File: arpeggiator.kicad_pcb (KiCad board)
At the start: 2 copper layers, 220 x 170 mm, 360 parts, among them J202 logic test header, J601 3.5mm mono line out, J701 PJ-102AH / 12V DC centre +, Q601 2N7002, Q602 MMBT3904, Q603 BSS84, Q604 MMBT3904, Q605 2N7002, Q606 MMBT3906, Q701 AO3401A, Q702 MMBT3906, Q703 MMBT3906, SW101 C, SW102 C sharp, SW103 D, SW104 D sharp, SW105 E, SW106 F, SW107 F sharp, SW108 G, SW109 G sharp, SW110 A, SW111 A sharp, SW112 B, SW113 start / stop, SW114 1 / 2 / 3 octaves, SW601 saw / pulse, U101 TLC555IDR, U102 TLC555IDR, U103 MCP100T-450I/TT, U201 74HC574, U202 74HC574, U203 74HC574, U204 74HC574, U205 74HC377, U206 74HC377, U211 74HC163, U212 74HC138, U213 74HC163, U214 74HC163, U215 74HC163, U216 CD74HC4067M, U221 74HC377, U222 74HC154, U301 74HC74, U302 74HC74, U303 74HC74, U401 74HC14, U402 74HC14, U403 74HC14, U404 74HC04, U405 74HC04, U406 74HC08, U407 74HC86, U408 74HC04, U409 74HC32, U410 74HC32, U411 74HC32, U412 74HC32, U413 74HC08, U414 74HC08, U415 74HC86, U416 74HC04, U417 74HC08, U418 74HC08, U419 74HC32, U420 74HC14, U421 74HC08, U422 74HC32, U423 74HC08, U424 74HC32, U425 74HC08, U501 OPA4192IDR, U502 ADG706BRUZ, U503 74HC4051D, U504 AS3340A, U601 TLC555IDR, U602 OPA4192IDR, U603 TL074HIDR, U604 LM13700M/NOPB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

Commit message: finish signal routing and clean up the traces
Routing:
- net PITCH0: track 0.00 -> 248.3 mm, vias 0 -> 7
- net PITCH1: track 0.00 -> 228.5 mm, vias 0 -> 9
- net PITCH3: track 0.00 -> 222.4 mm, vias 0 -> 10
- net PITCH2: track 0.00 -> 220.6 mm, vias 0 -> 2
- net OCTAVE0: track 0.00 -> 168.9 mm, vias 0 -> 4
- net TRIGGER: track 0.00 -> 167.5 mm, vias 0 -> 5
- net OCTAVE1: track 0.00 -> 155.2 mm, vias 0 -> 6
- net VALID: track 56.6 -> 195.7 mm, vias 4 -> 5
- net G060: track 0.00 -> 139.0 mm, vias 0 -> 8
- net +5V: track 1531.4 -> 1668.6 mm, vias 26 -> 57
- net N1: track 18.2 -> 151.6 mm, vias 2 -> 5
- net NEG_BAD: track 0.00 -> 118.5 mm, vias 0 -> 4
- net RESET5_N: track 0.00 -> 108.3 mm, vias 0 -> 6
- net G081: track 0.00 -> 99.4 mm, vias 0 -> 8
- net BUTTON_RC: track 27.6 -> 124.2 mm, vias 2 -> 5
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
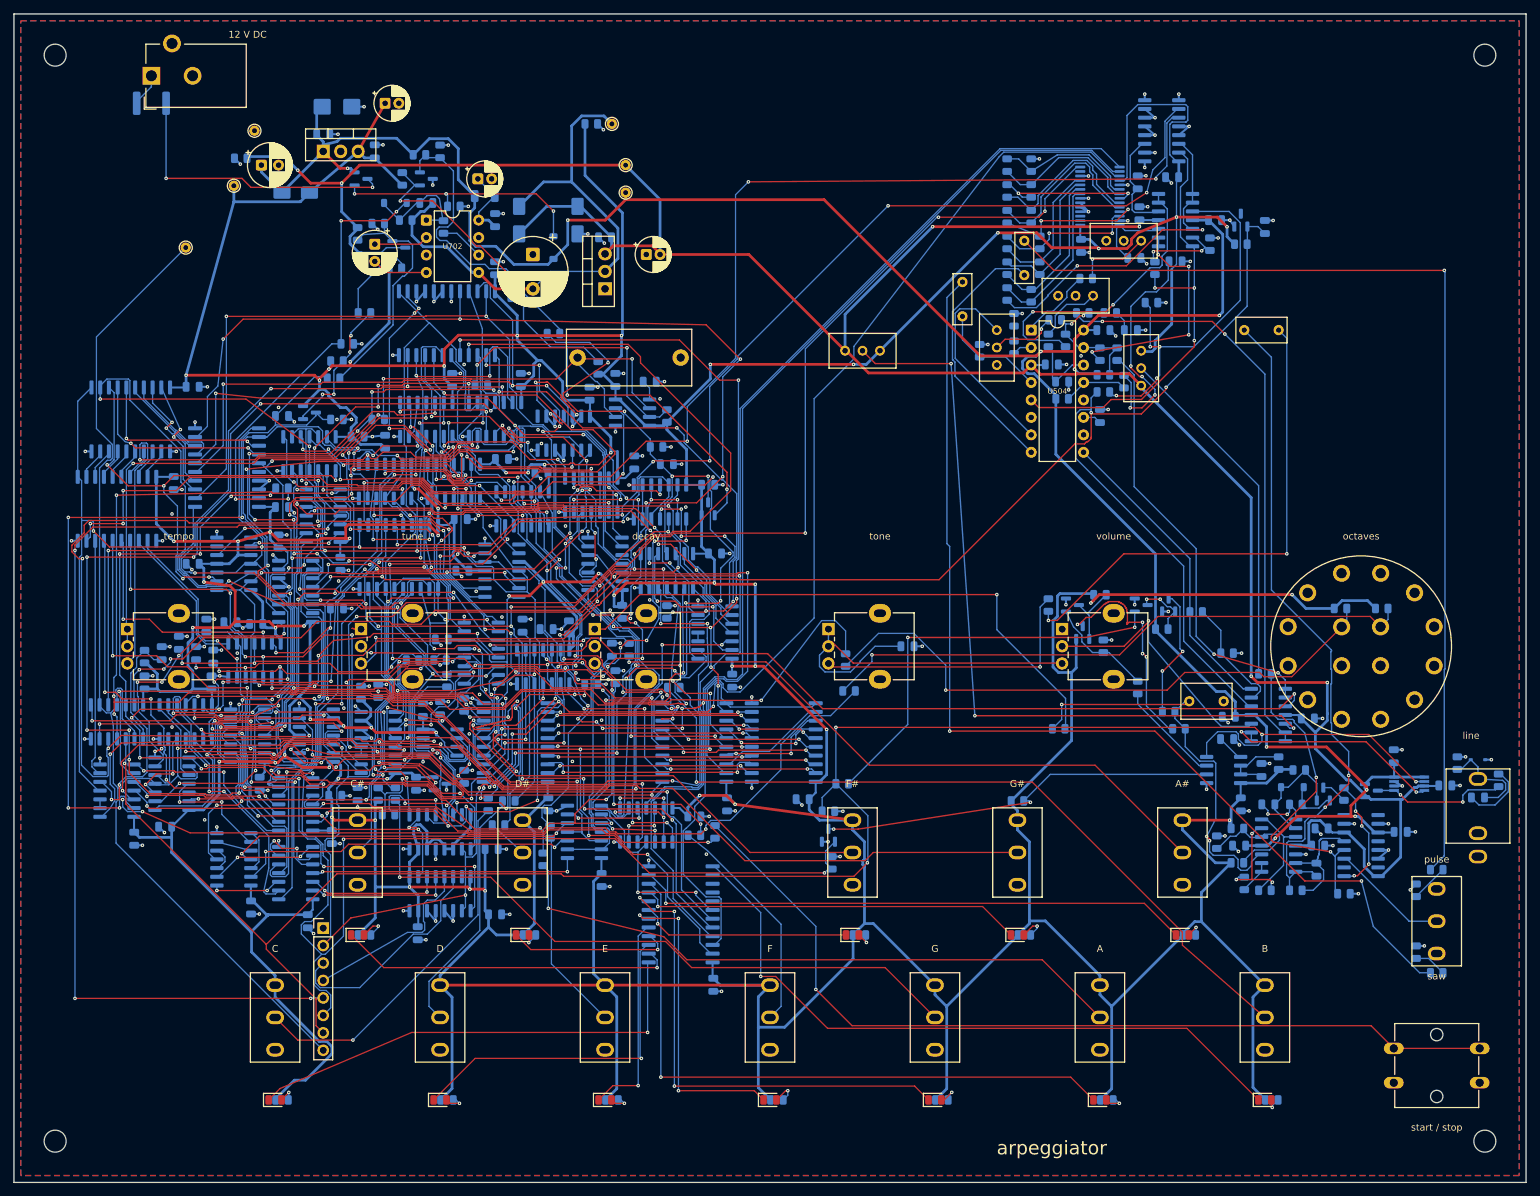
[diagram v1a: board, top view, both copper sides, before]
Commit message: connect ground pours and remove redundant routing
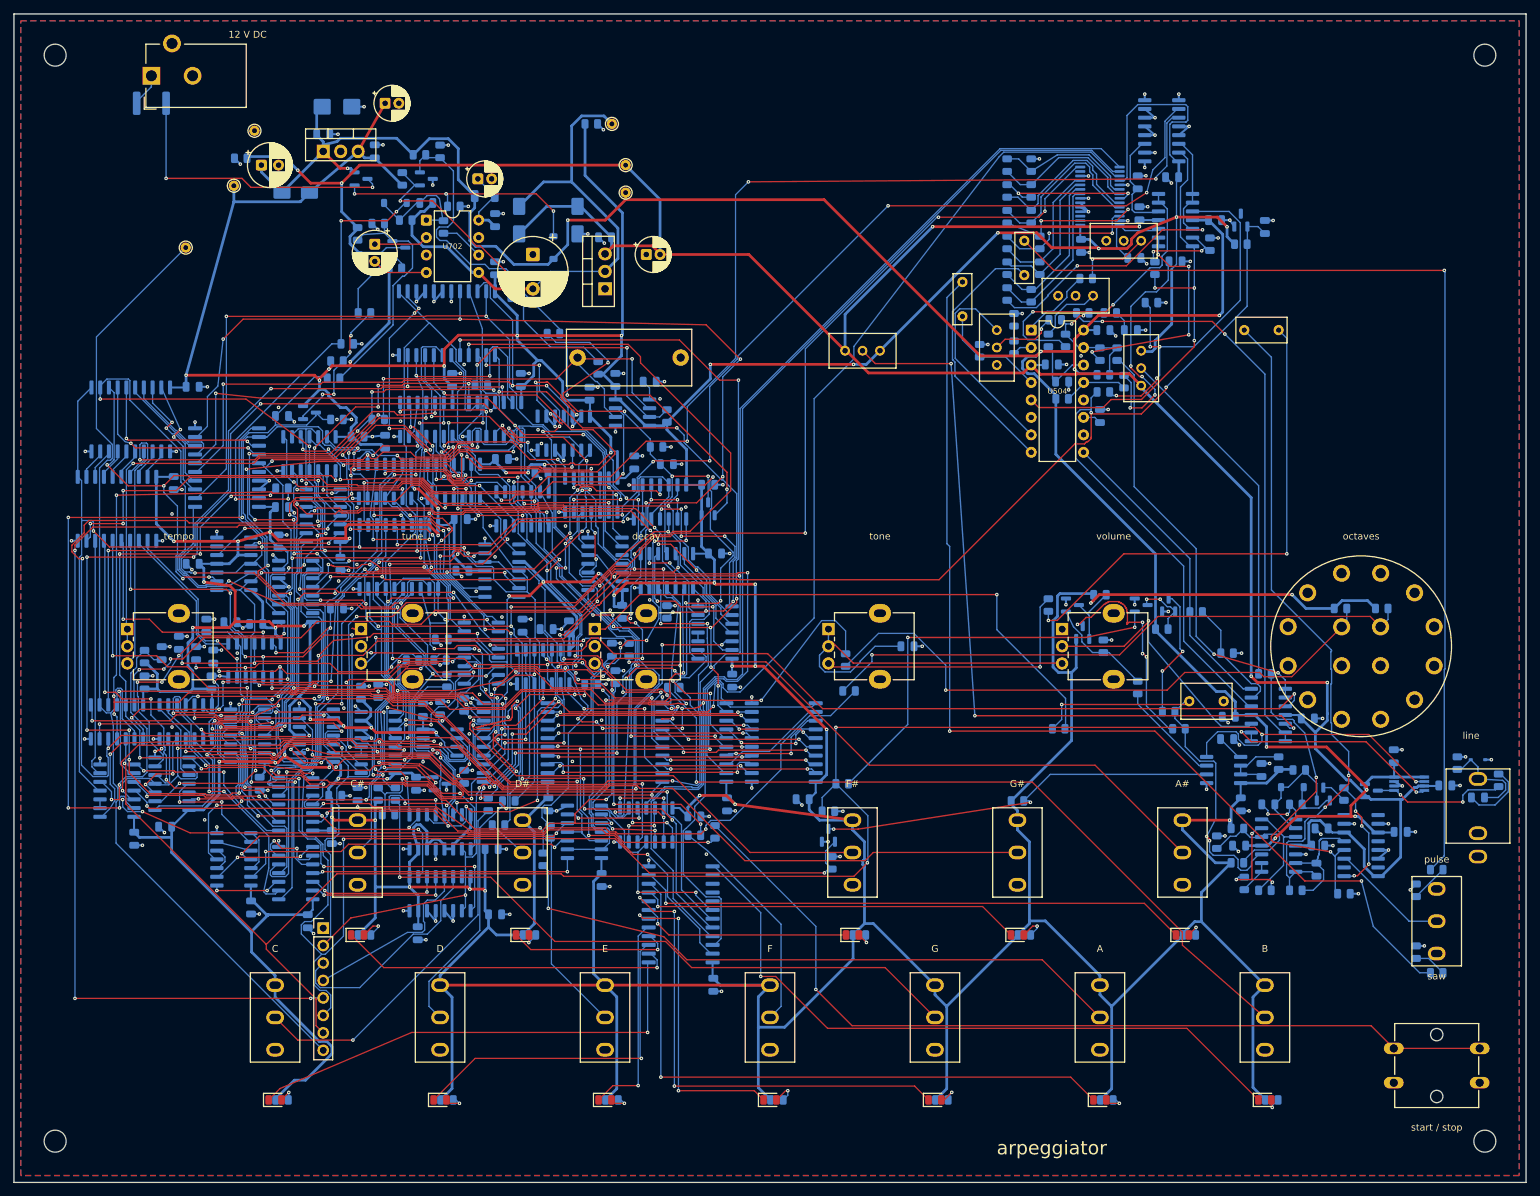
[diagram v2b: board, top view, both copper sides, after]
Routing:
- net FAST_CLK: track 358.8 -> 353.6 mm
- net ADVANCE: track 50.4 -> 47.2 mm
- net RANGE0: track 116.0 -> 113.0 mm
- net N3: track 152.4 -> 149.6 mm
- net RESET_N: track 295.1 -> 292.3 mm
- net RANGE1: track 134.0 -> 131.5 mm
- net N2: track 143.9 -> 141.4 mm
- net TIM161: track 130.0 -> 127.6 mm
- net PITCH1: track 228.5 -> 226.2 mm, vias 9 -> 8
- net RUN: track 158.8 -> 156.6 mm
- net NOTE_SNAP3: track 88.7 -> 86.7 mm
- net OCT_EN: track 63.4 -> 61.4 mm
- net IDLE: track 65.7 -> 63.8 mm
- net DIS151: track 52.7 -> 50.8 mm
- net VALID: track 195.7 -> 193.9 mm
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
